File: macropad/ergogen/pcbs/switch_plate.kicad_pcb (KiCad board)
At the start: 2 copper layers, 193.3 x 44.5 mm, 0 parts

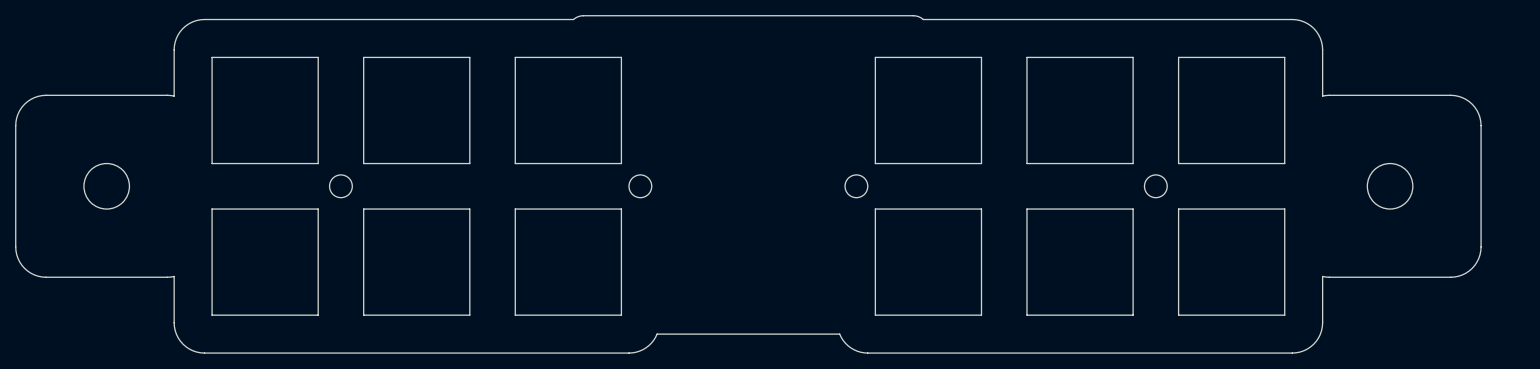
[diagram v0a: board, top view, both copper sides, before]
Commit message: batt connector space fix
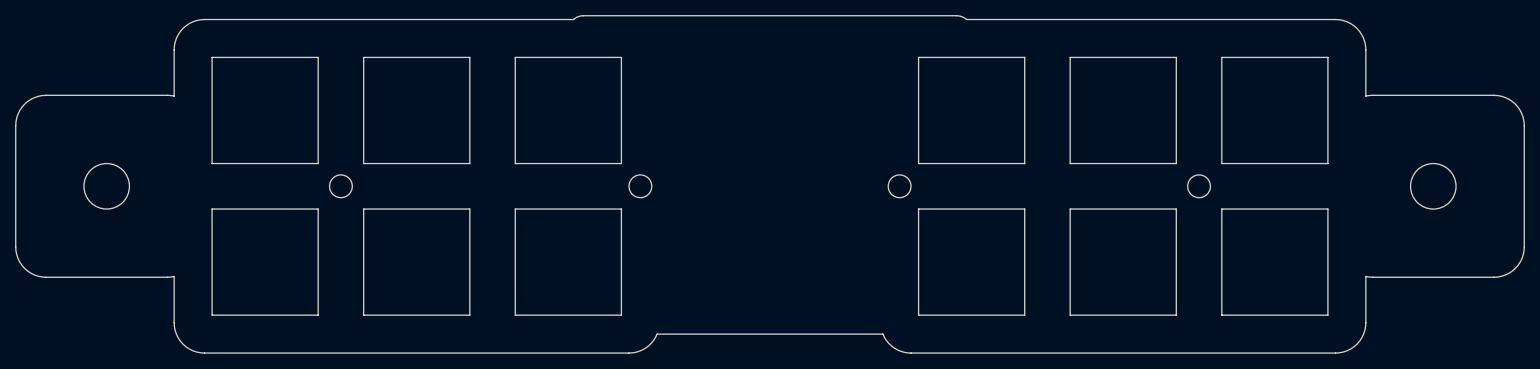
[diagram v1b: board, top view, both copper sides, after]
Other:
- board size 193.3 x 44.5 mm -> 199 x 44.5 mm

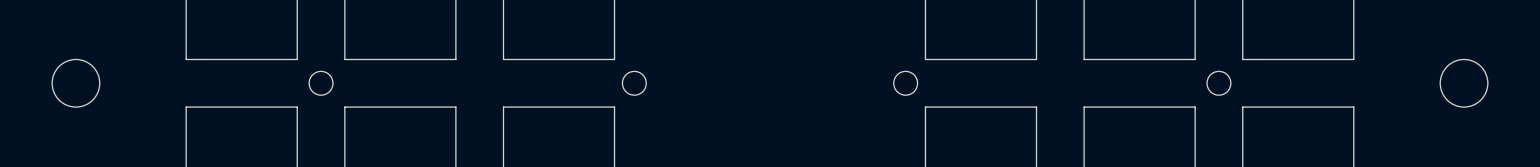
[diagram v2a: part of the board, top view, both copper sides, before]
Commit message: Ergogen: Updating assigned pins Ergogen: Renaming pins names to NiceNano Pings RMK: Updating assigned pins RMK: Always clear storage, temporary RMK: Trying to fix vial layout
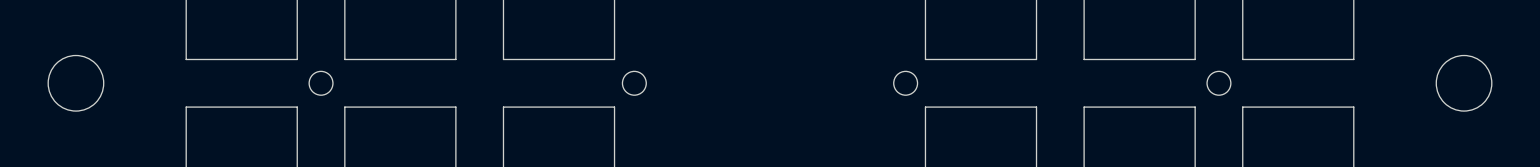
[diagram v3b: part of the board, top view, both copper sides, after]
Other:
- outline, holes or cut-outs redrawn
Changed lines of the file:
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@@
   (title_block
     (title "switch_plate")
-    (date "2026-03-06")
+    (date "2026-03-09")
     (rev "0.0.1")
     (company "pedroren")
@@
 (gr_line (start 200.2 93) (end 186.2 93) (layer Edge.Cuts) (stroke (width 0.15) (type default)))
 (gr_line (start 186.2 93) (end 186.2 107) (layer Edge.Cuts) (stroke (width 0.15) (type default)))
-(gr_circle (center 79.1 110) (end 82.1 110) (layer Edge.Cuts) (stroke (width 0.15) (type default)) (fill none))
-(gr_circle (center 254.1 110) (end 257.1 110) (layer Edge.Cuts) (stroke (width 0.15) (type default)) (fill none))
+(gr_circle (center 79.1 110) (end 82.6 110) (layer Edge.Cuts) (stroke (width 0.15) (type default)) (fill none))
+(gr_circle (center 254.1 110) (end 257.6 110) (layer Edge.Cuts) (stroke (width 0.15) (type default)) (fill none))
 (gr_circle (center 110 110) (end 111.5 110) (layer Edge.Cuts) (stroke (width 0.15) (type default)) (fill none))
 (gr_circle (center 149.5 110) (end 151 110) (layer Edge.Cuts) (stroke (width 0.15) (type default)) (fill none))

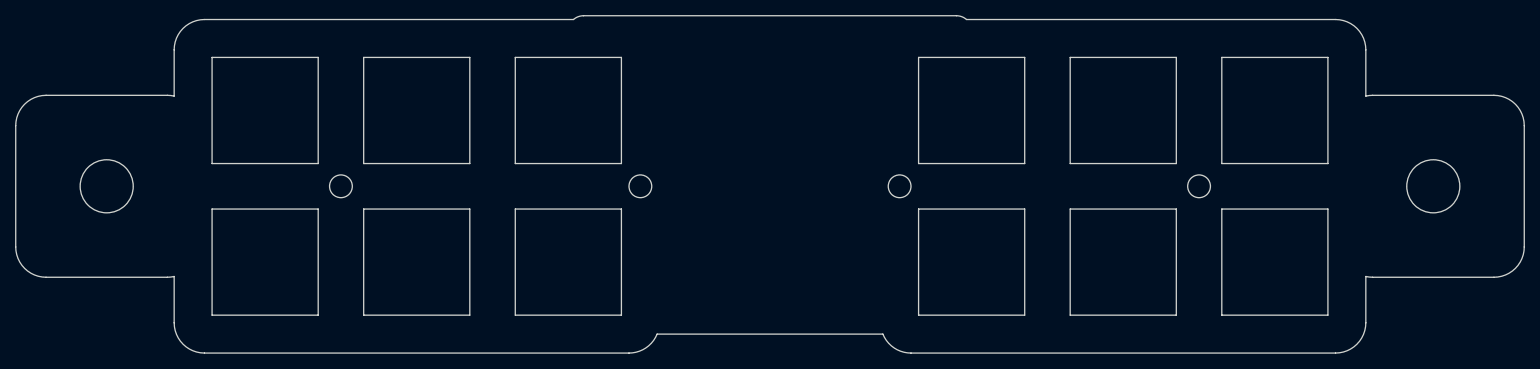
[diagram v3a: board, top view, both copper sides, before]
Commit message: Inner case verical spacing Cutout for USB, reset and power Switchplate sides support
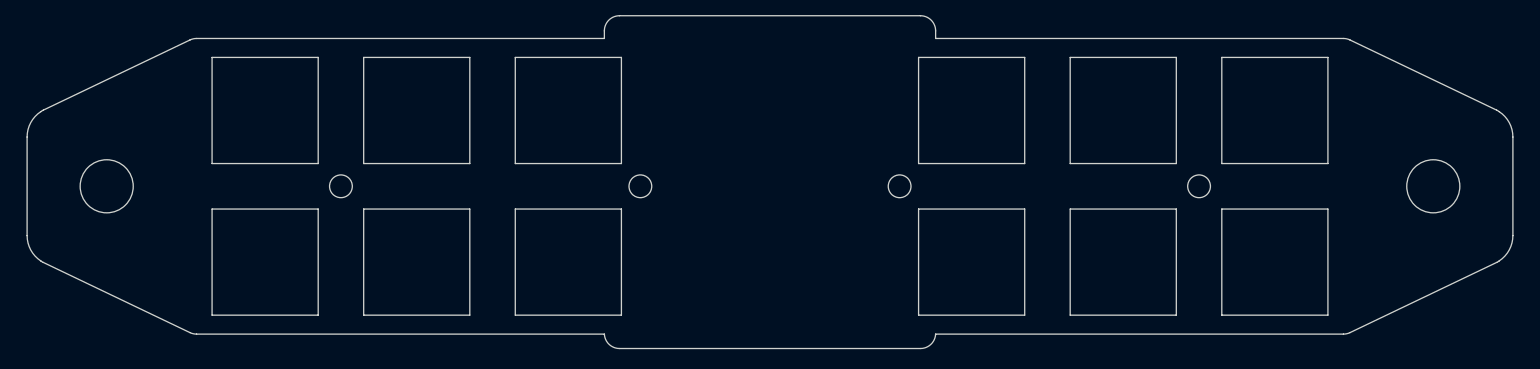
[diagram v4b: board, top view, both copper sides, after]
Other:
- board size 199 x 44.5 mm -> 196 x 43.9 mm
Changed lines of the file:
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@@
   (title_block
     (title "switch_plate")
-    (date "2026-03-09")
+    (date "2026-03-11")
     (rev "0.0.1")
     (company "pedroren")
@@
   )
   (net 0 "")
-  (gr_line (start 92 132) (end 148 132) (layer Edge.Cuts) (stroke (width 0.15) (type default)))
-(gr_line (start 88 128) (end 88 121.8974351) (layer Edge.Cuts) (stroke (width 0.15) (type default)))
-(gr_line (start 88 98.1025649) (end 88 92) (layer Edge.Cuts) (stroke (width 0.15) (type default)))
-(gr_arc (start 88 128) (mid 89.1715729 130.8284271) (end 92 132) (layer Edge.Cuts) (stroke (width 0.15) (type default)))
-(gr_line (start 92 88) (end 140.6771243 88) (layer Edge.Cuts) (stroke (width 0.15) (type default)))
-(gr_arc (start 92 88) (mid 89.1715729 89.1715729) (end 88 92) (layer Edge.Cuts) (stroke (width 0.15) (type default)))
-(gr_arc (start 148 132) (mid 150.236068 131.3166248) (end 151.7080992 129.5) (layer Edge.Cuts) (stroke (width 0.15) (type default)))
-(gr_line (start 185.2 132) (end 241.2 132) (layer Edge.Cuts) (stroke (width 0.15) (type default)))
-(gr_arc (start 241.2 132) (mid 244.0284271 130.8284271) (end 245.2 128) (layer Edge.Cuts) (stroke (width 0.15) (type default)))
-(gr_line (start 245.2 128) (end 245.2 121.8974351) (layer Edge.Cuts) (stroke (width 0.15) (type default)))
-(gr_line (start 245.2 98.1025649) (end 245.2 92) (layer Edge.Cuts) (stroke (width 0.15) (type default)))
-(gr_arc (start 245.2 92) (mid 244.0284271 89.1715729) (end 241.2 88) (layer Edge.Cuts) (stroke (width 0.15) (type default)))
-(gr_line (start 192.5228757 88) (end 241.2 88) (layer Edge.Cuts) (stroke (width 0.15) (type default)))
-(gr_arc (start 181.4919008 129.5) (mid 182.9639321 131.3166248) (end 185.2 132) (layer Edge.Cuts) (stroke (width 0.15) (type default)))
-(gr_line (start 71.1 122) (end 87.1 122) (layer Edge.Cuts) (stroke (width 0.15) (type default)))
-(gr_arc (start 87.1 122) (mid 87.5529127 121.974276) (end 88 121.8974351) (layer Edge.Cuts) (stroke (width 0.15) (type default)))
-(gr_arc (start 88 98.1025649) (mid 87.5529127 98.0257239) (end 87.1 98) (layer Edge.Cuts) (stroke (width 0.15) (type default)))
-(gr_line (start 87.1 98) (end 71.1 98) (layer Edge.Cuts) (stroke (width 0.15) (type default)))
-(gr_arc (start 71.1 98) (mid 68.2715729 99.1715729) (end 67.1 102) (layer Edge.Cuts) (stroke (width 0.15) (type default)))
-(gr_line (start 67.1 102) (end 67.1 118) (layer Edge.Cuts) (stroke (width 0.15) (type default)))
-(gr_arc (start 67.1 118) (mid 68.2715729 120.8284271) (end 71.1 122) (layer Edge.Cuts) (stroke (width 0.15) (type default)))
-(gr_line (start 246.1 122) (end 262.1 122) (layer Edge.Cuts) (stroke (width 0.15) (type default)))
-(gr_arc (start 262.1 122) (mid 264.9284271 120.8284271) (end 266.1 118) (layer Edge.Cuts) (stroke (width 0.15) (type default)))
-(gr_line (start 266.1 118) (end 266.1 102) (layer Edge.Cuts) (stroke (width 0.15) (type default)))
-(gr_arc (start 266.1 102) (mid 264.9284271 99.1715729) (end 262.1 98) (layer Edge.Cuts) (stroke (width 0.15) (type default)))
-(gr_line (start 262.1 98) (end 246.1 98) (layer Edge.Cuts) (stroke (width 0.15) (type default)))
-(gr_arc (start 246.1 98) (mid 245.64708729999998 98.025724) (end 245.2 98.1025649) (layer Edge.Cuts) (stroke (width 0.15) (type default)))
-(gr_arc (start 245.2 121.8974351) (mid 245.64708729999998 121.9742761) (end 246.1 122) (layer Edge.Cuts) (stroke (width 0.15) (type default)))
-(gr_line (start 142 87.5) (end 191.2 87.5) (layer Edge.Cuts) (stroke (width 0.15) (type default)))
-(gr_line (start 181.4919008 129.5) (end 151.7080992 129.5) (layer Edge.Cuts) (stroke (width 0.15) (type default)))
-(gr_arc (start 142 87.5) (mid 141.2928932 87.6291713) (end 140.6771243 88) (layer Edge.Cuts) (stroke (width 0.15) (type default)))
-(gr_arc (start 192.5228757 88) (mid 191.90710679999998 87.6291713) (end 191.2 87.5) (layer Edge.Cuts) (stroke (width 0.15) (type default)))
+  (gr_line (start 70.7367836389337 99.95608438328529) (end 90.09061564593371 90.69587768137143) (layer Edge.Cuts) (stroke (width 0.15) (type default)))
+(gr_line (start 90.953832007 90.5) (end 144.75 90.5) (layer Edge.Cuts) (stroke (width 0.15) (type default)))
+(gr_line (start 188.45 90.5) (end 242.246167993 90.5) (layer Edge.Cuts) (stroke (width 0.15) (type default)))
+(gr_line (start 243.10938435406626 90.69587768137143) (end 262.4632163610664 99.95608438328533) (layer Edge.Cuts) (stroke (width 0.15) (type default)))
+(gr_line (start 262.4632163610664 120.04391561671466) (end 243.1093843540663 129.30412231862857) (layer Edge.Cuts) (stroke (width 0.15) (type default)))
+(gr_line (start 90.953832007 129.5) (end 144.7525016 129.5) (layer Edge.Cuts) (stroke (width 0.15) (type default)))
+(gr_line (start 188.4474984 129.5) (end 242.246167993 129.5) (layer Edge.Cuts) (stroke (width 0.15) (type default)))
+(gr_line (start 90.09061564593368 129.30412231862857) (end 70.73678363893369 120.04391561671468) (layer Edge.Cuts) (stroke (width 0.15) (type default)))
+(gr_arc (start 90.953832007 90.5) (mid 90.51125130700001 90.5495841) (end 90.090615607 90.6958776) (layer Edge.Cuts) (stroke (width 0.15) (type default)))
+(gr_arc (start 243.109384393 90.6958776) (mid 242.688748693 90.549584) (end 242.246167993 90.5) (layer Edge.Cuts) (stroke (width 0.15) (type default)))
+(gr_arc (start 262.7902548 100.15294390191387) (mid 262.6314429 100.04669400191388) (end 262.4632164 99.95608430191388) (layer Edge.Cuts) (stroke (width 0.15) (type default)))
+(gr_arc (start 262.4632164 120.04391569808611) (mid 262.6314429 119.95330599808611) (end 262.7902548 119.84705609808611) (layer Edge.Cuts) (stroke (width 0.15) (type default)))
+(gr_arc (start 242.246167993 129.5) (mid 242.688748693 129.4504159) (end 243.109384393 129.3041224) (layer Edge.Cuts) (stroke (width 0.15) (type default)))
+(gr_arc (start 90.090615607 129.3041224) (mid 90.51125130700001 129.450416) (end 90.953832007 129.5) (layer Edge.Cuts) (stroke (width 0.15) (type default)))
+(gr_arc (start 70.40974519999999 119.84705609808611) (mid 70.56855709999999 119.95330599808611) (end 70.7367836 120.04391569808611) (layer Edge.Cuts) (stroke (width 0.15) (type default)))
+(gr_arc (start 70.7367836 99.95608430191386) (mid 70.56855709999999 100.04669400191386) (end 70.40974519999999 100.15294390191386) (layer Edge.Cuts) (stroke (width 0.15) (type default)))
+(gr_line (start 144.75 90.5) (end 144.75 89.5) (layer Edge.Cuts) (stroke (width 0.15) (type default)))
+(gr_line (start 146.75 87.5) (end 186.45 87.5) (layer Edge.Cuts) (stroke (width 0.15) (type default)))
+(gr_line (start 188.45 89.5) (end 188.45 90.5) (layer Edge.Cuts) (stroke (width 0.15) (type default)))
+(gr_line (start 186.45 131.4) (end 146.75 131.4) (layer Edge.Cuts) (stroke (width 0.15) (type default)))
+(gr_arc (start 146.75 87.5) (mid 145.3357864 88.0857864) (end 144.75 89.5) (layer Edge.Cuts) (stroke (width 0.15) (type default)))
+(gr_arc (start 188.45 89.5) (mid 187.8642136 88.0857864) (end 186.45 87.5) (layer Edge.Cuts) (stroke (width 0.15) (type default)))
+(gr_arc (start 186.45 131.4) (mid 187.82840489999998 130.8491377) (end 188.4474984 129.5) (layer Edge.Cuts) (stroke (width 0.15) (type default)))
+(gr_arc (start 144.7525016 129.5) (mid 145.3715951 130.8491376) (end 146.75 131.4) (layer Edge.Cuts) (stroke (width 0.15) (type default)))
+(gr_arc (start 70.40974519999999 100.152944) (mid 69.08140519999999 101.5975042) (end 68.6 103.5) (layer Edge.Cuts) (stroke (width 0.15) (type default)))
+(gr_line (start 68.6 103.5) (end 68.6 116.5) (layer Edge.Cuts) (stroke (width 0.15) (type default)))
+(gr_arc (start 68.6 116.5) (mid 69.08140519999999 118.4024958) (end 70.40974519999999 119.847056) (layer Edge.Cuts) (stroke (width 0.15) (type default)))
+(gr_arc (start 262.7902548 119.847056) (mid 264.11859480000004 118.4024958) (end 264.6 116.5) (layer Edge.Cuts) (stroke (width 0.15) (type default)))
+(gr_line (start 264.6 116.5) (end 264.6 103.5) (layer Edge.Cuts) (stroke (width 0.15) (type default)))
+(gr_arc (start 264.6 103.5) (mid 264.11859480000004 101.5975042) (end 262.7902548 100.152944) (layer Edge.Cuts) (stroke (width 0.15) (type default)))
+(gr_circle (center 110 110) (end 111.5 110) (layer Edge.Cuts) (stroke (width 0.15) (type default)) (fill none))
+(gr_circle (center 149.5 110) (end 151 110) (layer Edge.Cuts) (stroke (width 0.15) (type default)) (fill none))
+(gr_circle (center 223.2 110) (end 224.7 110) (layer Edge.Cuts) (stroke (width 0.15) (type default)) (fill none))
+(gr_circle (center 183.7 110) (end 185.2 110) (layer Edge.Cuts) (stroke (width 0.15) (type default)) (fill none))
 (gr_line (start 93 127) (end 107 127) (layer Edge.Cuts) (stroke (width 0.15) (type default)))
 (gr_line (start 107 127) (end 107 113) (layer Edge.Cuts) (stroke (width 0.15) (type default)))
@@
 (gr_circle (center 79.1 110) (end 82.6 110) (layer Edge.Cuts) (stroke (width 0.15) (type default)) (fill none))
 (gr_circle (center 254.1 110) (end 257.6 110) (layer Edge.Cuts) (stroke (width 0.15) (type default)) (fill none))
-(gr_circle (center 110 110) (end 111.5 110) (layer Edge.Cuts) (stroke (width 0.15) (type default)) (fill none))
-(gr_circle (center 149.5 110) (end 151 110) (layer Edge.Cuts) (stroke (width 0.15) (type default)) (fill none))
-(gr_circle (center 223.2 110) (end 224.7 110) (layer Edge.Cuts) (stroke (width 0.15) (type default)) (fill none))
-(gr_circle (center 183.7 110) (end 185.2 110) (layer Edge.Cuts) (stroke (width 0.15) (type default)) (fill none))
 )
